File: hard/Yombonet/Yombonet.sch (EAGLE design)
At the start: 28 parts, among them IC1 ATMEGA644-20PU, IC2 XC9572-PC44, IC3 LD1117, IC4 ESP-07ESP-07, Q3 16 MHz, X1 ZX-EDGE

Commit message: Version preliminar de la PCB (PR3)
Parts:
- ACTIV.: value (none) -> -
- renumbered LED1 to ACTIV.
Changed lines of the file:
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@@
 <class number="0" name="default" width="0.2032" drill="0">
 </class>
-<class number="1" name="ground" width="0.4064" drill="0">
+<class number="1" name="ground" width="0.254" drill="0">
 </class>
 <class number="2" name="power" width="0.4064" drill="0">
@@
 <part name="R7" library="resistor" deviceset="R-EU_" device="0207_10" value="10K"/>
 <part name="R8" library="resistor" deviceset="R-EU_" device="0207_10" value="300"/>
-<part name="LED1" library="led" deviceset="LED" device="3MM"/>
+<part name="ACTIV." library="led" deviceset="LED" device="3MM" value="-"/>
 </parts>
 <sheets>
@@
 <instance part="R7" gate="G$1" x="83.82" y="35.56" rot="R270"/>
 <instance part="R8" gate="G$1" x="226.06" y="68.58"/>
-<instance part="LED1" gate="G$1" x="233.68" y="68.58" rot="R90"/>
+<instance part="ACTIV." gate="G$1" x="233.68" y="68.58" rot="R90"/>
 </instances>
 <busses>
@@
 </segment>
 <segment>
-<pinref part="LED1" gate="G$1" pin="C"/>
+<pinref part="ACTIV." gate="G$1" pin="C"/>
 <wire x1="238.76" y1="68.58" x2="241.3" y2="68.58" width="0.1524" layer="91"/>
 <label x="241.3" y="68.58" size="1.27" layer="95" xref="yes"/>
@@
 </segment>
 </net>
-<net name="N$3" class="0">
+<net name="N$3" class="2">
 <segment>
 <pinref part="JP3" gate="G$1" pin="1"/>
@@
 </segment>
 </net>
-<net name="N$2" class="0">
-<segment>
-<pinref part="LED1" gate="G$1" pin="A"/>
+<net name="N$2" class="1">
+<segment>
+<pinref part="ACTIV." gate="G$1" pin="A"/>
 <pinref part="R8" gate="G$1" pin="2"/>
 </segment>

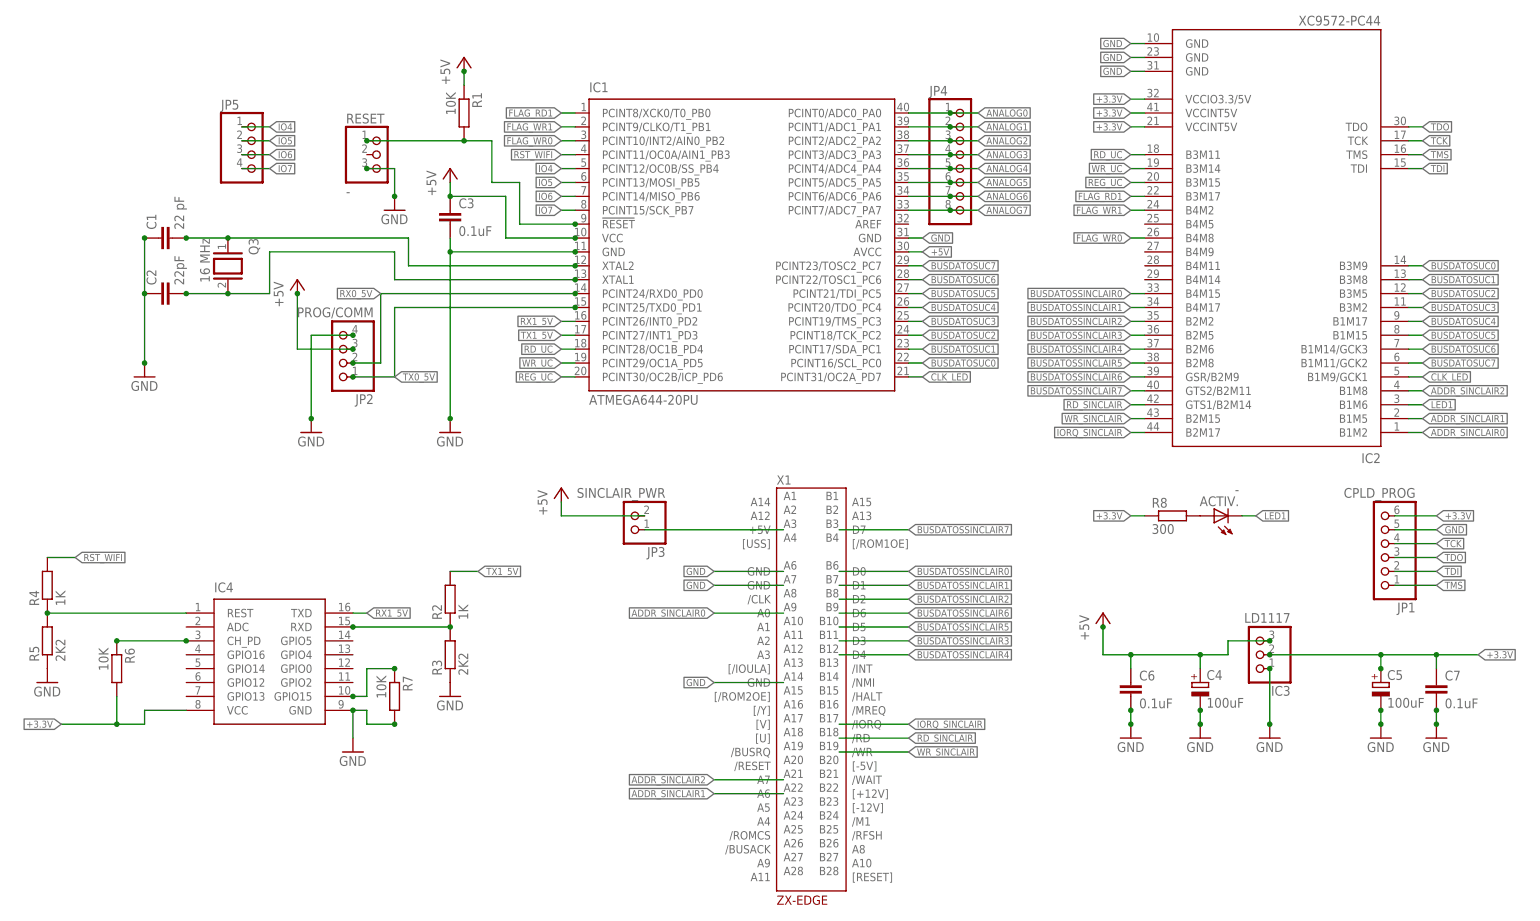
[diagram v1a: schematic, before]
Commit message: Esquematico: Cambiados varios conectores a uno solo de 2x6
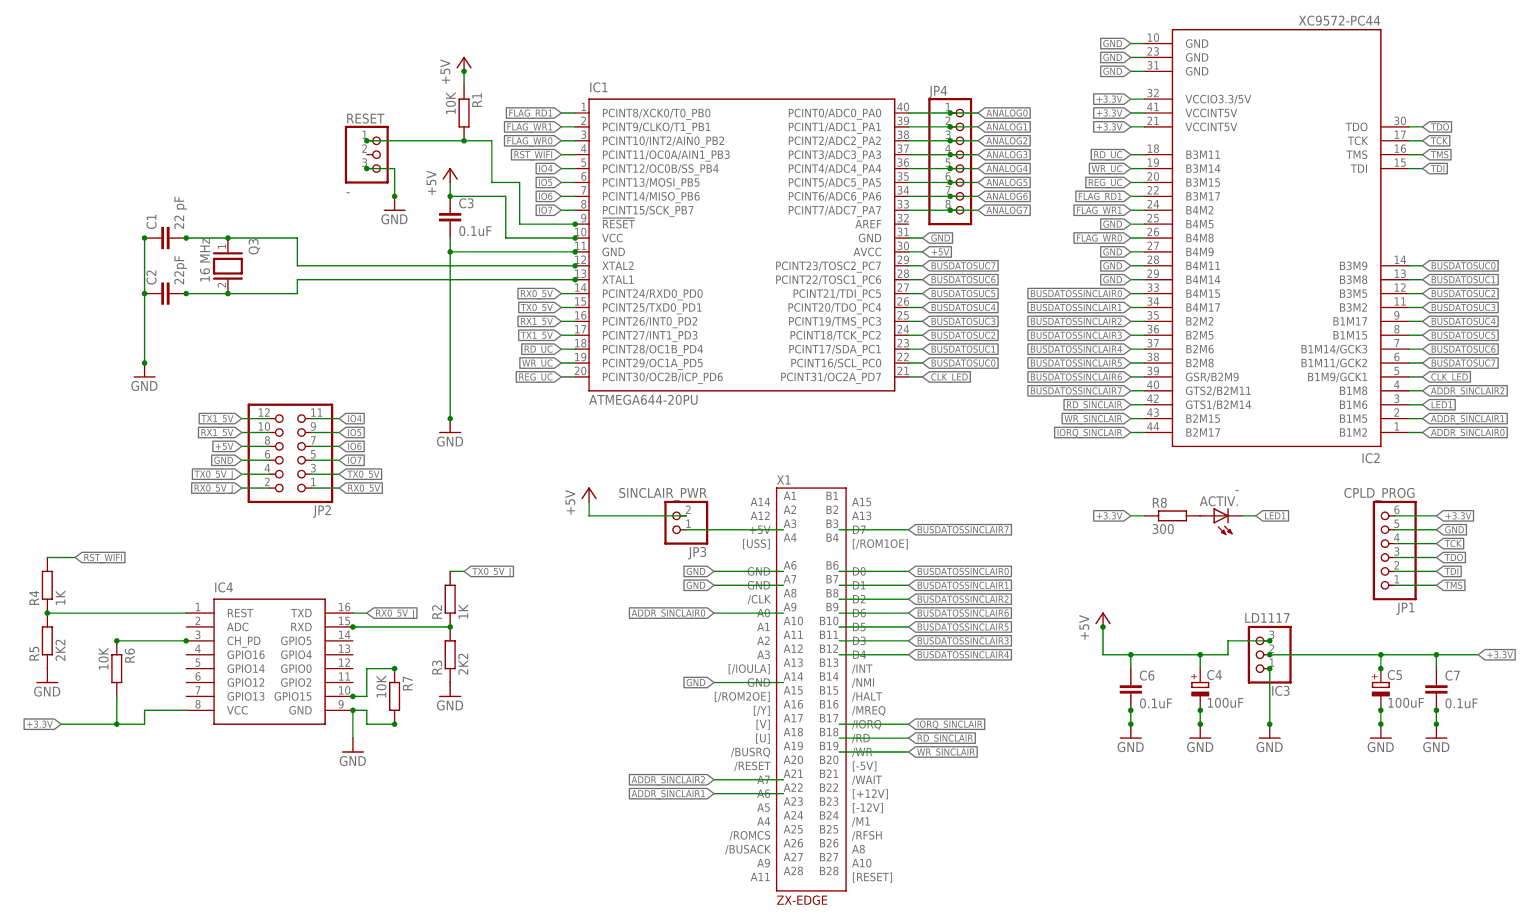
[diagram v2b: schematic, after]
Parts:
- removed JP5: (no value), pinhead:PINHD-1X4
- JP2: value PROG/COMM -> (none); device pinhead:PINHD-1X4 -> pinhead:PINHD-2X6
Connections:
- new net RX0_5V_J: IC4.TXD, JP2.2
- new net TX0_5V_J: JP2.4, R2.2
- net +5V: now also JP2.8; no longer JP2.3
- net GND: now also IC2.B4M11, IC2.B4M14, IC2.B4M5, IC2.B4M9, JP2.6; no longer JP2.4
- net IO4: now also JP2.11; no longer JP5.1
- net IO5: now also JP2.9; no longer JP5.2
- net IO6: now also JP2.7; no longer JP5.3
- net IO7: now also JP2.5; no longer JP5.4
- net RX0_5V: now also JP2.1; no longer JP2.2
- net RX1_5V: now also JP2.10; no longer IC4.TXD
- net TX0_5V: now also JP2.3; no longer JP2.1
- net TX1_5V: now also JP2.12; no longer R2.2
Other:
- moved on the sheet: JP3
